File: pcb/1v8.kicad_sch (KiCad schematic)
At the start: 6 parts, among them U14 AP3441SHE-7B

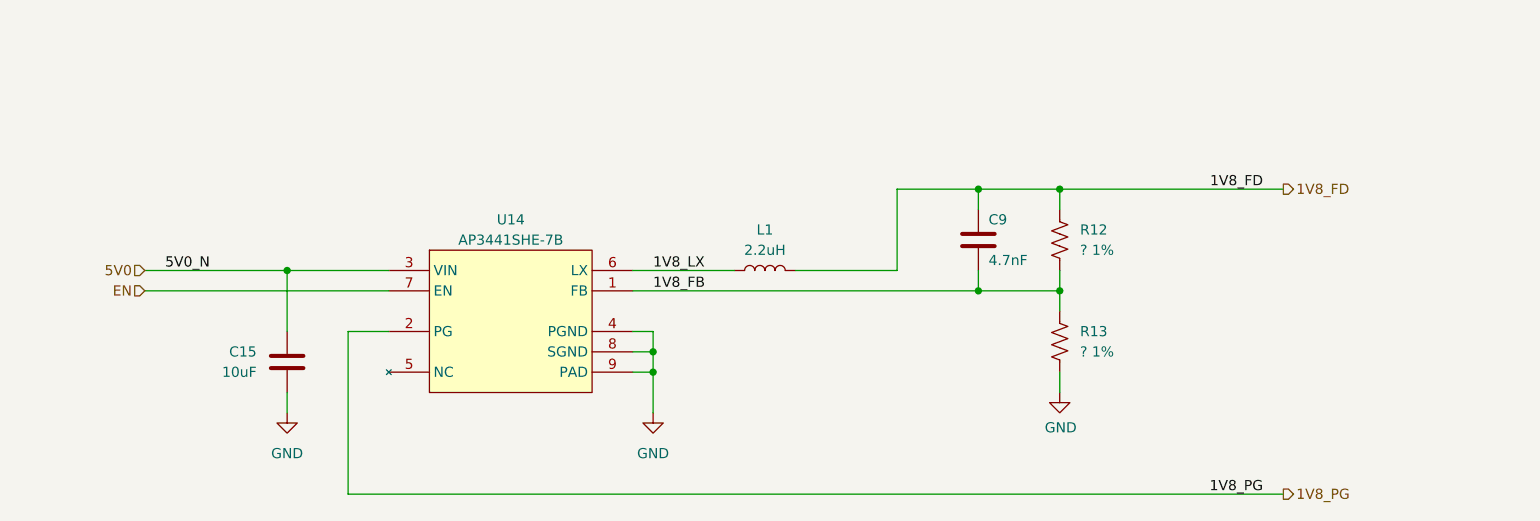
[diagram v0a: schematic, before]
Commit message: changes to power tree
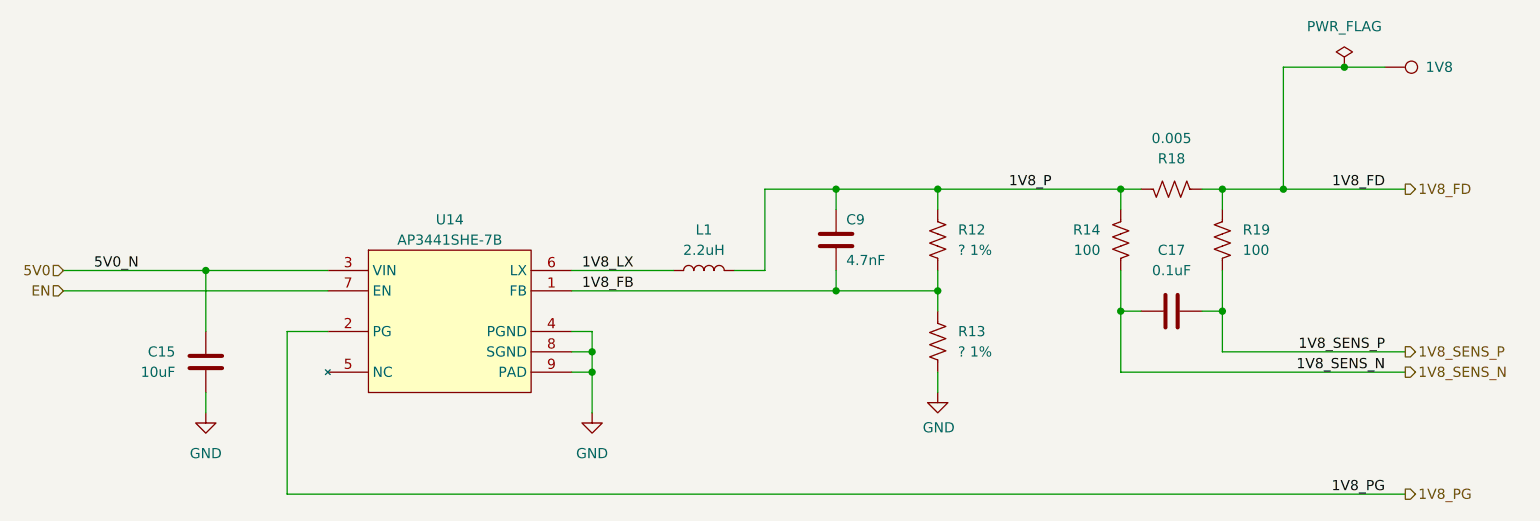
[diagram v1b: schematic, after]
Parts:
- added 1V8: TestPoint, TestPoint:TestPoint_Pad_D1.0mm, symbol library:TestPoint
- added C17: 0.1uF, Capacitor_SMD:C_0402_1005Metric, symbol library:C
- added R14, R19: 100, Resistor_SMD:R_0402_1005Metric, symbol library:R_US
- added R18: 0.005, Resistor_SMD:R_0603_1608Metric, symbol library:R_US
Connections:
- net 1V8_FD: now also 1V8.1, R18.1, R19.2; no longer C9.1, L1.2, R12.1
- new net 1V8_P: C9.1, L1.2, R12.1, R14.2, R18.2
- new net 1V8_SENS_N: C17.2, R14.1
- new net 1V8_SENS_P: C17.1, R19.1
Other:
- moved on the sheet: C15, C9, L1, R12, R13, U14

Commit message: moved stuff around, bom
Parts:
- R15: renamed from R12; value ? 1% -> 30K 1%
- R16: renamed from R13; value ? 1% -> 15K 1%
- renumbered C15 to C12, C9 to C13, C17 to C14, R14 to R17, U14 to U5
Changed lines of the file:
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@@
 		(at 76.2 93.98)
 		(diameter 0)
-		(color 0 0 0 0)
+		(color 255 0 0 1)
 	)
 	(junction
@@
 	(wire
 		(pts
-			(xy 91.44 101.6) (xy 86.36 101.6)
+			(xy 91.44 101.6) (xy 88.9 101.6)
 		)
 		(stroke
@@
 	(wire
 		(pts
-			(xy 86.36 101.6) (xy 86.36 121.92)
+			(xy 88.9 101.6) (xy 88.9 121.92)
 		)
 		(stroke
@@
 	(wire
 		(pts
-			(xy 86.36 121.92) (xy 226.06 121.92)
+			(xy 88.9 121.92) (xy 226.06 121.92)
 		)
 		(stroke
@@
 		(on_board yes)
 		(dnp no)
-		(property "Reference" "C15"
+		(property "Reference" "C12"
 			(at 72.39 104.1399 0)
 			(effects
@@
 			(project "RPi-HwAB-1"
 				(path "/e63e39d7-6ac0-4ffd-8aa3-1841a4541b55/f9ebb56c-78c7-42ac-bc19-ccbf788f5318/40f8c9cc-8de9-43ac-8cba-fe7ae095cfae"
-					(reference "C15")
+					(reference "C12")
 					(unit 1)
 				)
@@
 		(on_board yes)
 		(dnp no)
-		(property "Reference" "#PWR012"
+		(property "Reference" "#PWR019"
 			(at 167.64 115.57 0)
 			(effects
@@
 			(project "RPi-HwAB-1"
 				(path "/e63e39d7-6ac0-4ffd-8aa3-1841a4541b55/f9ebb56c-78c7-42ac-bc19-ccbf788f5318/40f8c9cc-8de9-43ac-8cba-fe7ae095cfae"
-					(reference "#PWR012")
+					(reference "#PWR019")
 					(unit 1)
 				)
@@
 		(on_board yes)
 		(dnp no)
-		(property "Reference" "C9"
+		(property "Reference" "C13"
 			(at 156.21 87.63 0)
 			(effects
@@
 			(project "RPi-HwAB-1"
 				(path "/e63e39d7-6ac0-4ffd-8aa3-1841a4541b55/f9ebb56c-78c7-42ac-bc19-ccbf788f5318/40f8c9cc-8de9-43ac-8cba-fe7ae095cfae"
-					(reference "C9")
+					(reference "C13")
 					(unit 1)
 				)
@@
 		(dnp no)
 		(fields_autoplaced yes)
-		(property "Reference" "#FLG05"
+		(property "Reference" "#FLG04"
 			(at 218.44 66.675 0)
 			(effects
@@
 			(project "RPi-HwAB-1"
 				(path "/e63e39d7-6ac0-4ffd-8aa3-1841a4541b55/f9ebb56c-78c7-42ac-bc19-ccbf788f5318/40f8c9cc-8de9-43ac-8cba-fe7ae095cfae"
-					(reference "#FLG05")
+					(reference "#FLG04")
 					(unit 1)
 				)
@@
 		(dnp no)
 		(fields_autoplaced yes)
-		(property "Reference" "#PWR040"
+		(property "Reference" "#PWR017"
 			(at 76.2 118.11 0)
 			(effects
@@
 			(project "RPi-HwAB-1"
 				(path "/e63e39d7-6ac0-4ffd-8aa3-1841a4541b55/f9ebb56c-78c7-42ac-bc19-ccbf788f5318/40f8c9cc-8de9-43ac-8cba-fe7ae095cfae"
-					(reference "#PWR040")
+					(reference "#PWR017")
 					(unit 1)
 				)
@@
 		(on_board yes)
 		(dnp no)
-		(property "Reference" "R12"
+		(property "Reference" "R15"
 			(at 170.18 88.9 0)
 			(effects
@@
 			)
 		)
-		(property "Value" "? 1%"
+		(property "Value" "30K 1%"
 			(at 170.18 91.44 0)
 			(effects
@@
 			(project "RPi-HwAB-1"
 				(path "/e63e39d7-6ac0-4ffd-8aa3-1841a4541b55/f9ebb56c-78c7-42ac-bc19-ccbf788f5318/40f8c9cc-8de9-43ac-8cba-fe7ae095cfae"
-					(reference "R12")
+					(reference "R15")
 					(unit 1)
 				)
@@
 		(dnp no)
 		(fields_autoplaced yes)
-		(property "Reference" "C17"
+		(property "Reference" "C14"
 			(at 196.85 91.44 90)
 			(effects
@@
 			(project "RPi-HwAB-1"
 				(path "/e63e39d7-6ac0-4ffd-8aa3-1841a4541b55/f9ebb56c-78c7-42ac-bc19-ccbf788f5318/40f8c9cc-8de9-43ac-8cba-fe7ae095cfae"
-					(reference "C17")
+					(reference "C14")
 					(unit 1)
 				)
@@
 		(dnp no)
 		(fields_autoplaced yes)
-		(property "Reference" "R14"
+		(property "Reference" "R17"
 			(at 187.96 88.8999 0)
 			(effects
@@
 			(project "RPi-HwAB-1"
 				(path "/e63e39d7-6ac0-4ffd-8aa3-1841a4541b55/f9ebb56c-78c7-42ac-bc19-ccbf788f5318/40f8c9cc-8de9-43ac-8cba-fe7ae095cfae"
-					(reference "R14")
+					(reference "R17")
 					(unit 1)
 				)
@@
 		(dnp no)
 		(fields_autoplaced yes)
-		(property "Reference" "U14"
+		(property "Reference" "U5"
 			(at 106.68 87.63 0)
 			(effects
@@
 			(project "RPi-HwAB-1"
 				(path "/e63e39d7-6ac0-4ffd-8aa3-1841a4541b55/f9ebb56c-78c7-42ac-bc19-ccbf788f5318/40f8c9cc-8de9-43ac-8cba-fe7ae095cfae"
-					(reference "U14")
+					(reference "U5")
 					(unit 1)
 				)
@@
 		(dnp no)
 		(fields_autoplaced yes)
-		(property "Reference" "#PWR013"
+		(property "Reference" "#PWR018"
 			(at 124.46 118.11 0)
 			(effects
@@
 			(project "RPi-HwAB-1"
 				(path "/e63e39d7-6ac0-4ffd-8aa3-1841a4541b55/f9ebb56c-78c7-42ac-bc19-ccbf788f5318/40f8c9cc-8de9-43ac-8cba-fe7ae095cfae"
-					(reference "#PWR013")
+					(reference "#PWR018")
 					(unit 1)
 				)
@@
 		(on_board yes)
 		(dnp no)
-		(property "Reference" "R13"
+		(property "Reference" "R16"
 			(at 170.18 101.6 0)
 			(effects
@@
 			)
 		)
-		(property "Value" "? 1%"
+		(property "Value" "15K 1%"
 			(at 170.18 104.14 0)
 			(effects
@@
 			(project "RPi-HwAB-1"
 				(path "/e63e39d7-6ac0-4ffd-8aa3-1841a4541b55/f9ebb56c-78c7-42ac-bc19-ccbf788f5318/40f8c9cc-8de9-43ac-8cba-fe7ae095cfae"
-					(reference "R13")
+					(reference "R16")
 					(unit 1)
 				)

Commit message: decoupling
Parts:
- R17, R19: value 100 -> 10; Manufacturer (none) -> YAGEO; Manufacturer Product Number (none) -> RC0402FR-0710RL
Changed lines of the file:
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@@
+	(wire
+		(pts
+			(xy 190.5 93.98) (xy 190.5 99.06)
+		)
+		(stroke
+			(width 0)
+			(type default)
+		)
+	)
 	(wire
 		(pts
@@
 			(width 0)
 			(type solid)
-		)
-	)
-	(wire
-		(pts
-			(xy 190.5 93.98) (xy 190.5 99.06)
-		)
-		(stroke
-			(width 0)
-			(type default)
 		)
 	)
@@
 				(path "/e63e39d7-6ac0-4ffd-8aa3-1841a4541b55/f9ebb56c-78c7-42ac-bc19-ccbf788f5318/40f8c9cc-8de9-43ac-8cba-fe7ae095cfae"
 					(reference "C13")
-					(unit 1)
-				)
-			)
-		)
-	)
-	(symbol
-		(lib_id "library:R_US")
-		(at 203.2 90.17 0)
-		(mirror x)
-		(unit 1)
-		(exclude_from_sim no)
-		(in_bom yes)
-		(on_board yes)
-		(dnp no)
-		(property "Reference" "R19"
-			(at 205.74 88.9 0)
-			(effects
-				(font
-					(size 1.27 1.27)
-				)
-				(justify left)
-			)
-		)
-		(property "Value" "100"
-			(at 205.74 91.44 0)
-			(effects
-				(font
-					(size 1.27 1.27)
-				)
-				(justify left)
-			)
-		)
-		(property "Footprint" "Resistor_SMD:R_0402_1005Metric"
-			(at 204.216 89.916 90)
-			(effects
-				(font
-					(size 1.27 1.27)
-				)
-				(hide yes)
-			)
-		)
-		(property "Datasheet" "~"
-			(at 203.2 90.17 0)
-			(effects
-				(font
-					(size 1.27 1.27)
-				)
-				(hide yes)
-			)
-		)
-		(property "Description" "Resistor, US symbol"
-			(at 203.2 90.17 0)
-			(effects
-				(font
-					(size 1.27 1.27)
-				)
-				(hide yes)
-			)
-		)
-		(property "Name" ""
-			(at 203.2 90.17 0)
-			(effects
-				(font
-					(size 1.27 1.27)
-				)
-				(hide yes)
-			)
-		)
-		(pin "1"
-		)
-		(pin "2"
-		)
-		(instances
-			(project "RPi-HwAB-1"
-				(path "/e63e39d7-6ac0-4ffd-8aa3-1841a4541b55/f9ebb56c-78c7-42ac-bc19-ccbf788f5318/40f8c9cc-8de9-43ac-8cba-fe7ae095cfae"
-					(reference "R19")
 					(unit 1)
 				)
@@
 	(symbol
 		(lib_id "library:R_US")
-		(at 190.5 90.17 0)
-		(mirror x)
+		(at 190.5 90.17 180)
 		(unit 1)
 		(exclude_from_sim no)
@@
 		(on_board yes)
 		(dnp no)
-		(fields_autoplaced yes)
 		(property "Reference" "R17"
-			(at 187.96 88.8999 0)
-			(effects
-				(font
-					(size 1.27 1.27)
-				)
-				(justify right)
-			)
-		)
-		(property "Value" "100"
-			(at 187.96 91.4399 0)
-			(effects
-				(font
-					(size 1.27 1.27)
-				)
-				(justify right)
+			(at 187.96 88.9 0)
+			(effects
+				(font
+					(size 1.27 1.27)
+				)
+				(justify left)
+			)
+		)
+		(property "Value" "10"
+			(at 187.96 91.44 0)
+			(effects
+				(font
+					(size 1.27 1.27)
+				)
+				(justify left)
 			)
 		)
 		(property "Footprint" "Resistor_SMD:R_0402_1005Metric"
-			(at 191.516 89.916 90)
+			(at 189.484 89.916 90)
 			(effects
 				(font
@@
 			)
 		)
-		(property "Description" "Resistor, US symbol"
+		(property "Description" "RES 10 OHM 1% 1/16W 0402"
+			(at 190.5 90.17 0)
+			(effects
+				(font
+					(size 1.27 1.27)
+				)
+				(hide yes)
+			)
+		)
+		(property "Manufacturer" "YAGEO"
+			(at 190.5 90.17 0)
+			(effects
+				(font
+					(size 1.27 1.27)
+				)
+				(hide yes)
+			)
+		)
+		(property "Manufacturer Product Number" "RC0402FR-0710RL"
 			(at 190.5 90.17 0)
 			(effects
@@
 					(unit 1)
 				)
+			)
+		)
+	)
+	(symbol
+		(lib_id "library:R_US")
+		(at 203.2 90.17 180)
+		(unit 1)
+		(exclude_from_sim no)
+		(in_bom yes)
+		(on_board yes)
+		(dnp no)
+		(property "Reference" "R19"
+			(at 205.74 88.9 0)
+			(effects
+				(font
+					(size 1.27 1.27)
+				)
+				(justify right)
+			)
+		)
+		(property "Value" "10"
+			(at 205.74 91.44 0)
+			(effects
+				(font
+					(size 1.27 1.27)
+				)
+				(justify right)
+			)
+		)
+		(property "Footprint" "Resistor_SMD:R_0402_1005Metric"
+			(at 202.184 89.916 90)
+			(effects
+				(font
+					(size 1.27 1.27)
+				)
+				(hide yes)
+			)
+		)
+		(property "Datasheet" "~"
+			(at 203.2 90.17 0)
+			(effects
+				(font
+					(size 1.27 1.27)
+				)
+				(hide yes)
+			)
+		)
+		(property "Description" "RES 10 OHM 1% 1/16W 0402"
+			(at 203.2 90.17 0)
+			(effects
+				(font
+					(size 1.27 1.27)
+				)
+				(hide yes)
+			)
+		)
+		(property "Manufacturer" "YAGEO"
+			(at 203.2 90.17 0)
+			(effects
+				(font
+					(size 1.27 1.27)
+				)
+				(hide yes)
+			)
+		)
+		(property "Manufacturer Product Number" "RC0402FR-0710RL"
+			(at 203.2 90.17 0)
+			(effects
+				(font
+					(size 1.27 1.27)
+				)
+				(hide yes)
+			)
+		)
+		(property "Name" ""
+			(at 203.2 90.17 0)
+			(effects
+				(font
+					(size 1.27 1.27)
+				)
+				(hide yes)
+			)
+		)
+		(pin "1"
+		)
+		(pin "2"
+		)
+		(instances
+			(project "RPi-HwAB-1"
+				(path "/e63e39d7-6ac0-4ffd-8aa3-1841a4541b55/f9ebb56c-78c7-42ac-bc19-ccbf788f5318/40f8c9cc-8de9-43ac-8cba-fe7ae095cfae"
+					(reference "R19")
+					(unit 1)
+				)

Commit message: bom
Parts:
- 1V8: now left out of the parts list
- C12: footprint (none) -> Capacitor_SMD:C_0402_1005Metric; Manufacturer (none) -> Murata Electronics; Manufacturer Product Number (none) -> GRM155R61A106ME11D; Part Description (none) -> CAP CER 10UF 10V X5R 0402
- C13: Part Description (none) -> CAP CER 0402 4.7NF 50V X7R 5%
- C14: Manufacturer (none) -> KEMET; Manufacturer Product Number (none) -> C0402C104K4RACTU; Part Description (none) -> CAP CER 0.1UF 16V X7R 0402
- L1: footprint Inductor_SMD:L_Vishay_IHLP-1616 -> Inductor_SMD:L_Bourns_SRP1245A; Manufacturer Vishay Dale -> Bourns Inc.; Manufacturer Product Number IHLP1616BZER1R0M01 -> SRP1265A-2R2M; Part Description (none) -> FIXED IND 2.2UH 22A 4.2 MOHM SMD
- R16: renamed from R15; Manufacturer Product Number CRCW040210K0FKED -> CRCW040230K0FKED; Part Description (none) -> RES 30K OHM 1% 1/16W 0402
- R17: renamed from R16; Manufacturer Product Number CRCW04022K20FKED -> CRCW040215K0FKED; Part Description (none) -> RES 15K OHM 1% 1/16W 0402
- R18: renamed from R17; Part Description (none) -> RES 10 OHM 1% 1/16W 0402
- R19: renamed from R18; footprint Resistor_SMD:R_0603_1608Metric -> Resistor_SMD:R_1206_3216Metric; Manufacturer (none) -> Vishay Dale; Manufacturer Product Number (none) -> WSLP12065L000FEA; Part Description (none) -> RES 0.005 OHM 1% 1W 1206
- R20: renamed from R19; Part Description (none) -> RES 10 OHM 1% 1/16W 0402
- U5: Part Description (none) -> IC REG BUCK ADJ 3A UDFN20208
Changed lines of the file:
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@@
 			)
 		)
-		(property "Footprint" ""
+		(property "Footprint" "Capacitor_SMD:C_0402_1005Metric"
 			(at 77.1652 109.22 0)
 			(effects
@@
 			)
 		)
+		(property "Manufacturer" "Murata Electronics"
+			(at 76.2 105.41 0)
+			(effects
+				(font
+					(size 1.27 1.27)
+				)
+				(hide yes)
+			)
+		)
+		(property "Manufacturer Product Number" "GRM155R61A106ME11D"
+			(at 76.2 105.41 0)
+			(effects
+				(font
+					(size 1.27 1.27)
+				)
+				(hide yes)
+			)
+		)
+		(property "Part Description" "CAP CER 10UF 10V X5R 0402"
+			(at 76.2 105.41 0)
+			(effects
+				(font
+					(size 1.27 1.27)
+				)
+				(hide yes)
+			)
+		)
 		(pin "2"
 		)
@@
 		(unit 1)
 		(exclude_from_sim no)
-		(in_bom yes)
+		(in_bom no)
 		(on_board yes)
 		(dnp no)
@@
 			)
 		)
+		(property "Name" ""
+			(at 223.52 68.58 0)
+			(effects
+				(font
+					(size 1.27 1.27)
+				)
+				(hide yes)
+			)
+		)
 		(pin "1"
 		)
@@
 			)
 		)
-		(property "Datasheet" ""
+		(property "Datasheet" "~"
 			(at 154.94 90.17 0)
 			(effects
@@
 		)
 		(property "Manufacturer Product Number" "C0402C472J5RECTU"
+			(at 154.94 90.17 0)
+			(effects
+				(font
+					(size 1.27 1.27)
+				)
+				(hide yes)
+			)
+		)
+		(property "Part Description" "CAP CER 0402 4.7NF 50V X7R 5%"
 			(at 154.94 90.17 0)
 			(effects
@@
 		(on_board yes)
 		(dnp no)
-		(property "Reference" "R18"
+		(property "Reference" "R19"
 			(at 196.85 80.01 90)
 			(effects
@@
 			)
 		)
-		(property "Footprint" "Resistor_SMD:R_0603_1608Metric"
+		(property "Footprint" "Resistor_SMD:R_1206_3216Metric"
 			(at 196.596 82.804 90)
 			(effects
@@
 			)
 		)
+		(property "Manufacturer" "Vishay Dale"
+			(at 196.85 83.82 90)
+			(effects
+				(font
+					(size 1.27 1.27)
+				)
+				(hide yes)
+			)
+		)
+		(property "Manufacturer Product Number" "WSLP12065L000FEA"
+			(at 196.85 83.82 90)
+			(effects
+				(font
+					(size 1.27 1.27)
+				)
+				(hide yes)
+			)
+		)
+		(property "Part Description" "RES 0.005 OHM 1% 1W 1206"
+			(at 196.85 83.82 90)
+			(effects
+				(font
+					(size 1.27 1.27)
+				)
+				(hide yes)
+			)
+		)
 		(pin "1"
 		)
@@
 			(project "RPi-HwAB-1"
 				(path "/e63e39d7-6ac0-4ffd-8aa3-1841a4541b55/f9ebb56c-78c7-42ac-bc19-ccbf788f5318/40f8c9cc-8de9-43ac-8cba-fe7ae095cfae"
-					(reference "R18")
+					(reference "R19")
 					(unit 1)
 				)
@@
 		(on_board yes)
 		(dnp no)
-		(property "Reference" "R15"
+		(property "Reference" "R16"
 			(at 170.18 88.9 0)
 			(effects
@@
 			)
 		)
-		(property "Datasheet" ""
+		(property "Datasheet" "~"
 			(at 167.64 90.17 0)
 			(effects
@@
 			)
 		)
-		(property "Manufacturer Product Number" "CRCW040210K0FKED"
+		(property "Manufacturer Product Number" "CRCW040230K0FKED"
 			(at 167.64 90.17 0)
 			(effects
@@
 			)
 		)
+		(property "Part Description" "RES 30K OHM 1% 1/16W 0402"
+			(at 167.64 90.17 0)
+			(effects
+				(font
+					(size 1.27 1.27)
+				)
+				(hide yes)
+			)
+		)
 		(pin "1"
 		)
@@
 			(project "RPi-HwAB-1"
 				(path "/e63e39d7-6ac0-4ffd-8aa3-1841a4541b55/f9ebb56c-78c7-42ac-bc19-ccbf788f5318/40f8c9cc-8de9-43ac-8cba-fe7ae095cfae"
-					(reference "R15")
+					(reference "R16")
 					(unit 1)
 				)
@@
 			)
 		)
-		(property "Footprint" "Inductor_SMD:L_Vishay_IHLP-1616"
+		(property "Footprint" "Inductor_SMD:L_Bourns_SRP1245A"
 			(at 138.43 93.98 0)
 			(effects
@@
 			)
 		)
-		(property "Datasheet" ""
+		(property "Datasheet" "~"
 			(at 138.43 93.98 0)
 			(effects
@@
 			)
 		)
-		(property "Manufacturer" "Vishay Dale"
+		(property "Manufacturer" "Bourns Inc."
 			(at 138.43 93.98 90)
 			(effects
@@
 			)
 		)
-		(property "Manufacturer Product Number" "IHLP1616BZER1R0M01"
+		(property "Manufacturer Product Number" "SRP1265A-2R2M"
+			(at 138.43 93.98 90)
+			(effects
+				(font
+					(size 1.27 1.27)
+				)
+				(hide yes)
+			)
+		)
+		(property "Part Description" "FIXED IND 2.2UH 22A 4.2 MOHM SMD"
 			(at 138.43 93.98 90)
 			(effects
@@
 			)
 		)
+		(property "Manufacturer" "KEMET"
+			(at 196.85 99.06 90)
+			(effects
+				(font
+					(size 1.27 1.27)
+				)
+				(hide yes)
+			)
+		)
+		(property "Manufacturer Product Number" "C0402C104K4RACTU"
+			(at 196.85 99.06 90)
+			(effects
+				(font
+					(size 1.27 1.27)
+				)
+				(hide yes)
+			)
+		)
+		(property "Part Description" "CAP CER 0.1UF 16V X7R 0402"
+			(at 196.85 99.06 90)
+			(effects
+				(font
+					(size 1.27 1.27)
+				)
+				(hide yes)
+			)
+		)
 		(pin "1"
 		)
@@
 		(on_board yes)
 		(dnp no)
-		(property "Reference" "R17"
+		(property "Reference" "R18"
 			(at 187.96 88.9 0)
 			(effects
@@
 			)
 		)
+		(property "Part Description" "RES 10 OHM 1% 1/16W 0402"
+			(at 190.5 90.17 0)
+			(effects
+				(font
+					(size 1.27 1.27)
+				)
+				(hide yes)
+			)
+		)
 		(pin "1"
 		)
@@
 			(project "RPi-HwAB-1"
 				(path "/e63e39d7-6ac0-4ffd-8aa3-1841a4541b55/f9ebb56c-78c7-42ac-bc19-ccbf788f5318/40f8c9cc-8de9-43ac-8cba-fe7ae095cfae"
-					(reference "R17")
+					(reference "R18")
 					(unit 1)
 				)
@@
 			)
 		)
+		(property "Part Description" "IC REG BUCK ADJ 3A UDFN20208"
+			(at 106.68 101.6 0)
+			(effects
+				(font
+					(size 1.27 1.27)
+				)
+				(hide yes)
+			)
+		)
 		(pin "8"
 		)
@@
 		(on_board yes)
 		(dnp no)
-		(property "Reference" "R16"
+		(property "Reference" "R17"
 			(at 170.18 101.6 0)
 			(effects
@@
 			)
 		)
-		(property "Datasheet" ""
+		(property "Datasheet" "~"
 			(at 167.64 102.87 0)
 			(effects
@@
 			)
 		)
-		(property "Manufacturer Product Number" "CRCW04022K20FKED"
+		(property "Manufacturer Product Number" "CRCW040215K0FKED"
 			(at 167.64 102.87 0)
 			(effects
@@
 			)
 		)
+		(property "Part Description" "RES 15K OHM 1% 1/16W 0402"
+			(at 167.64 102.87 0)
+			(effects
+				(font
+					(size 1.27 1.27)
+				)
+				(hide yes)
+			)
+		)
 		(pin "1"
 		)
@@
 			(project "RPi-HwAB-1"
 				(path "/e63e39d7-6ac0-4ffd-8aa3-1841a4541b55/f9ebb56c-78c7-42ac-bc19-ccbf788f5318/40f8c9cc-8de9-43ac-8cba-fe7ae095cfae"
-					(reference "R16")
+					(reference "R17")
 					(unit 1)
 				)
@@
 		(on_board yes)
 		(dnp no)
-		(property "Reference" "R19"
+		(property "Reference" "R20"
 			(at 205.74 88.9 0)
 			(effects
@@
 			)
 		)
+		(property "Part Description" "RES 10 OHM 1% 1/16W 0402"
+			(at 203.2 90.17 0)
+			(effects
+				(font
+					(size 1.27 1.27)
+				)
+				(hide yes)
+			)
+		)
 		(pin "1"
 		)
@@
 			(project "RPi-HwAB-1"
 				(path "/e63e39d7-6ac0-4ffd-8aa3-1841a4541b55/f9ebb56c-78c7-42ac-bc19-ccbf788f5318/40f8c9cc-8de9-43ac-8cba-fe7ae095cfae"
-					(reference "R19")
-					(unit 1)
-				)
+					(reference "R20")
+					(unit 1)
+				)
